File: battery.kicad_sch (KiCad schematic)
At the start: 42 parts, among them IC2 XB8089D, J1 USB_C_Receptacle, U3 BQ24092DGQR, U4 TPS61085DGKR, U5 TPS259621DDAT

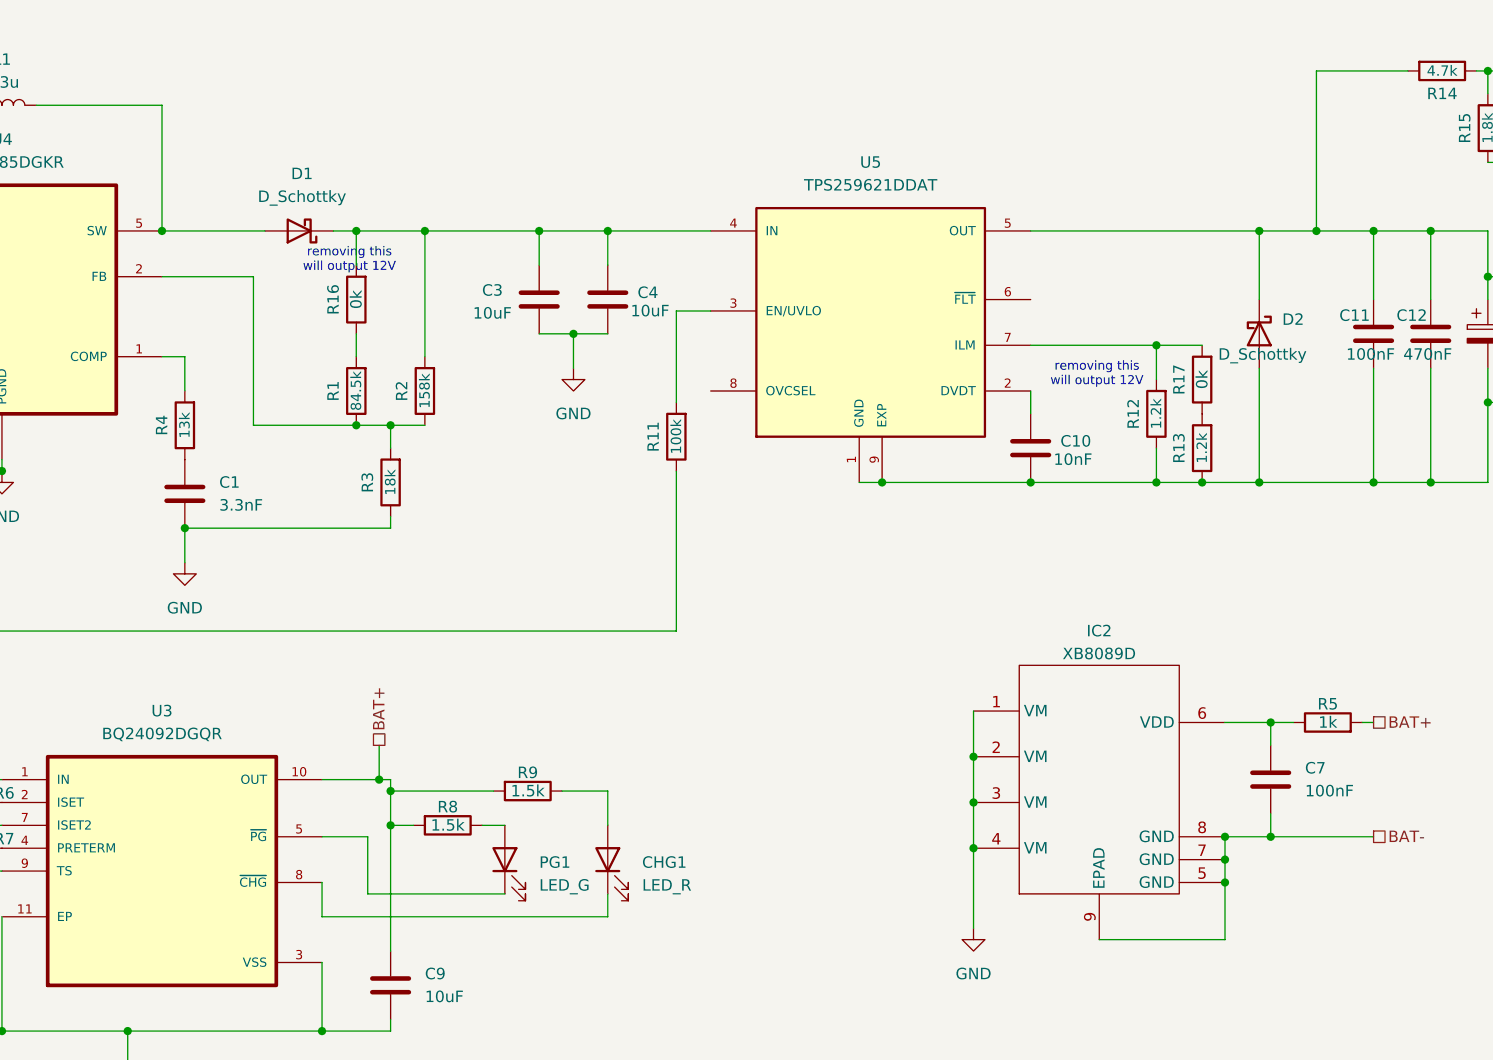
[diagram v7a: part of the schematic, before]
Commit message: move all backside components to front and make it work for jlc basic components
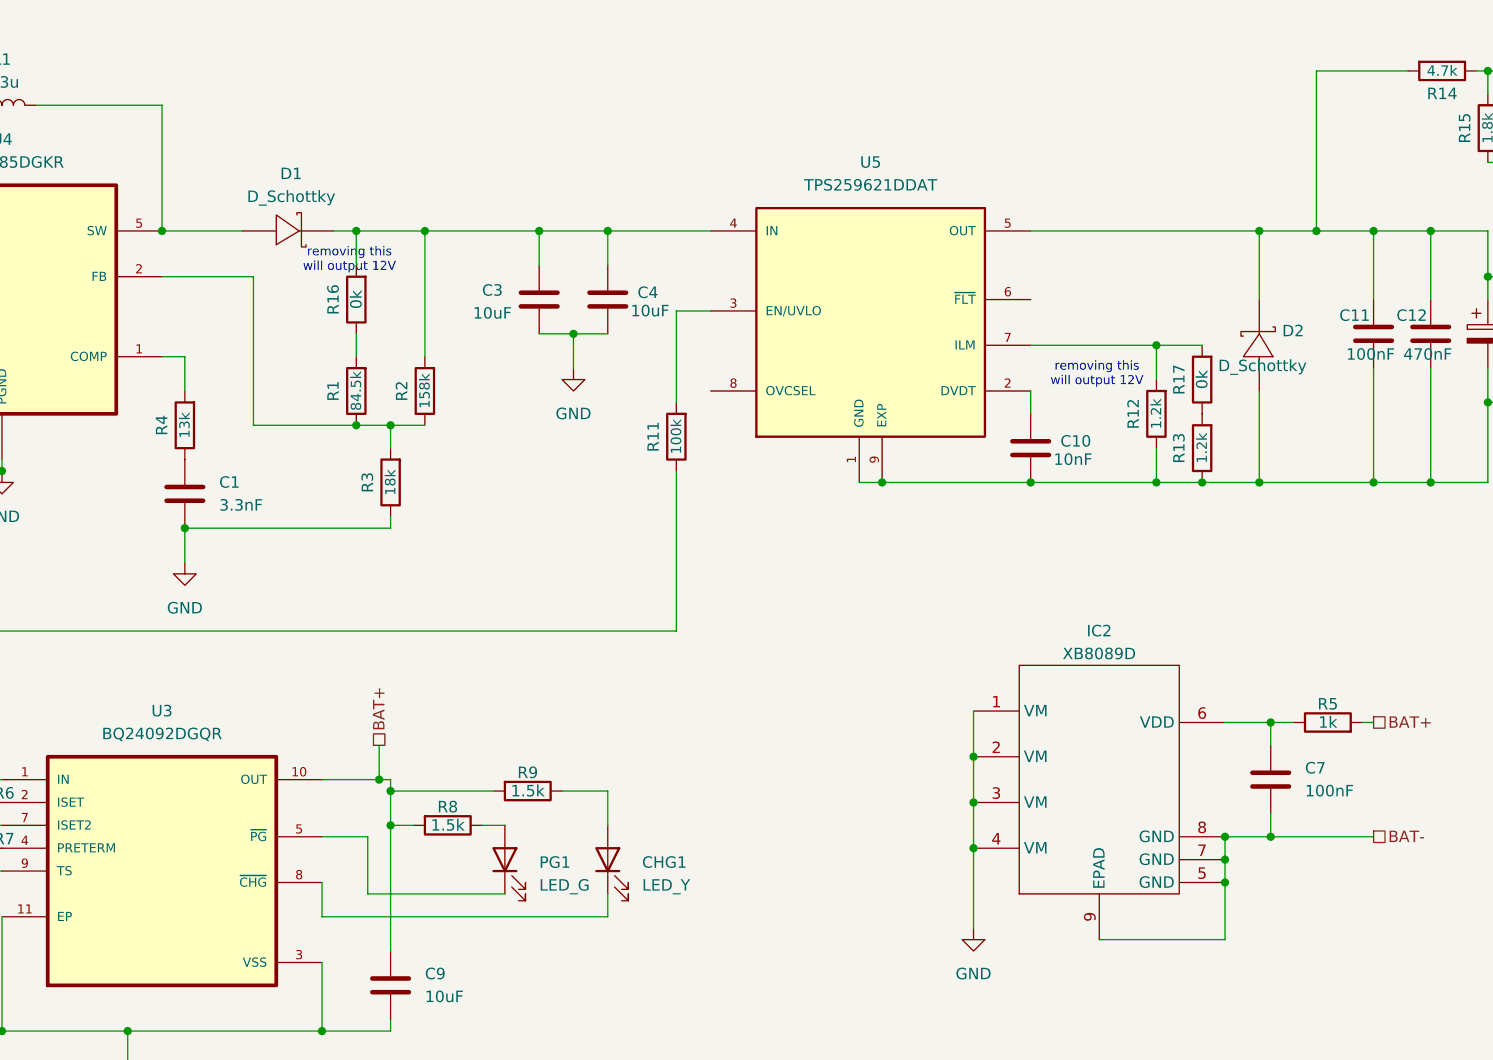
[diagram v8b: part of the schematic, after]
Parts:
- 12V1: footprint LED_SMD:LED_1206_3216Metric -> LED_SMD:LED_0603_1608Metric
- C1: footprint Capacitor_SMD:C_1206_3216Metric -> Capacitor_SMD:C_0603_1608Metric
- CHG1: value LED_R -> LED_Y; footprint LED_SMD:LED_1206_3216Metric -> LED_SMD:LED_0805_2012Metric
- D1, D2: footprint Diode_SMD:D_1206_3216Metric -> Schottky_Diode:SMA_L4.2-W2.6-LS5.3-RD; symbol Device:D_Schottky -> Schottky_diode:SS14; LCSC Part Name (none) -> 电压:40V 电流:1A; Manufacturer (none) -> MDD(辰达半导体); Manufacturer Part (none) -> SS14; Supplier (none) -> LCSC; Supplier Part (none) -> C2480
- PG1: footprint LED_SMD:LED_1206_3216Metric -> LED_SMD:LED_0805_2012Metric
- R12, R13, R8, R9: footprint Resistor_SMD:R_1206_3216Metric -> Resistor_SMD:R_0805_2012Metric
- R15, R3, R4: footprint Resistor_SMD:R_1206_3216Metric -> Resistor_SMD:R_0603_1608Metric
